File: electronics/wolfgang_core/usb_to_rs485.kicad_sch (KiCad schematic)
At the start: 34 parts

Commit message: Footprints hinzugefügt
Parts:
- U2: renamed from U?; footprint (none) -> Package_QFP:LQFP-64_10x10mm_P0.5mm
- U3, U4, U5, U6: renamed from U?; footprint (none) -> Package_SO:SOIC-8_3.9x4.9mm_P1.27mm
- gave numbers to parts that had none: 23
- renumbered D5 to D1, D6 to D2, D1 to D3, D2 to D4, D3 to D5, D4 to D6
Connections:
- net +5V: now reaches C10.1, U3.8 (VCC)
- net +5V: now also C11.1, C12.1, C13.1, U4.8 (VCC), U5.8 (VCC), U6.8 (VCC)

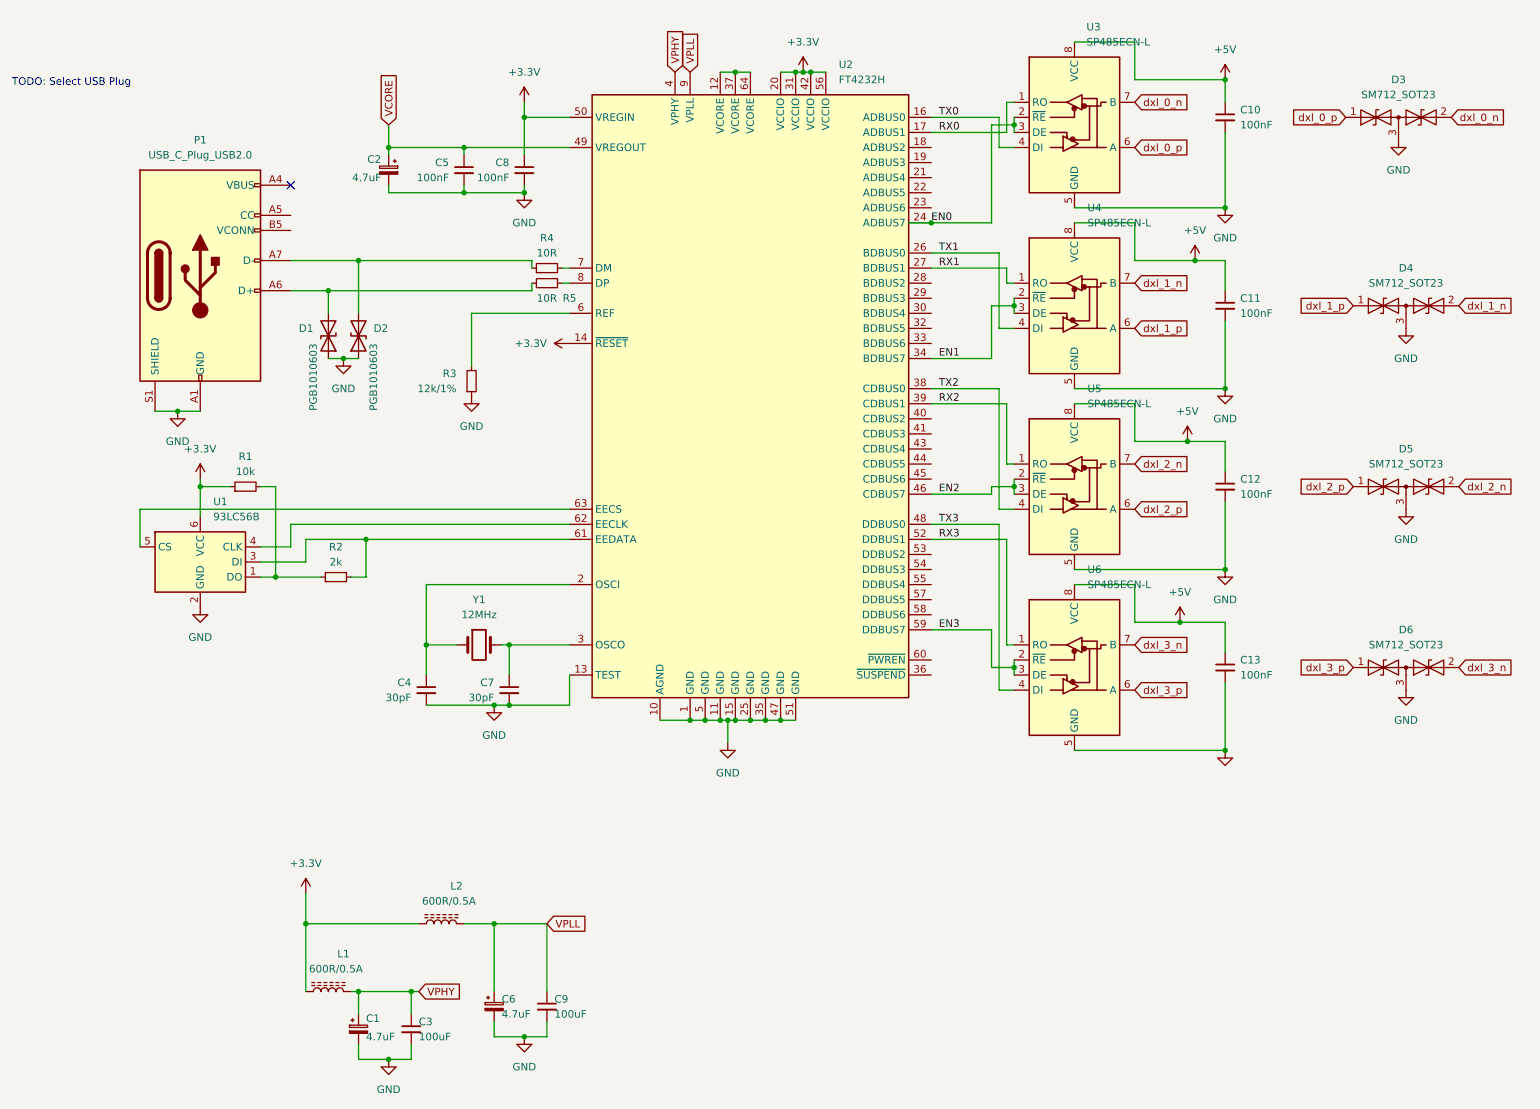
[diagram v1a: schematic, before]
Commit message: Assign almost all Footprints
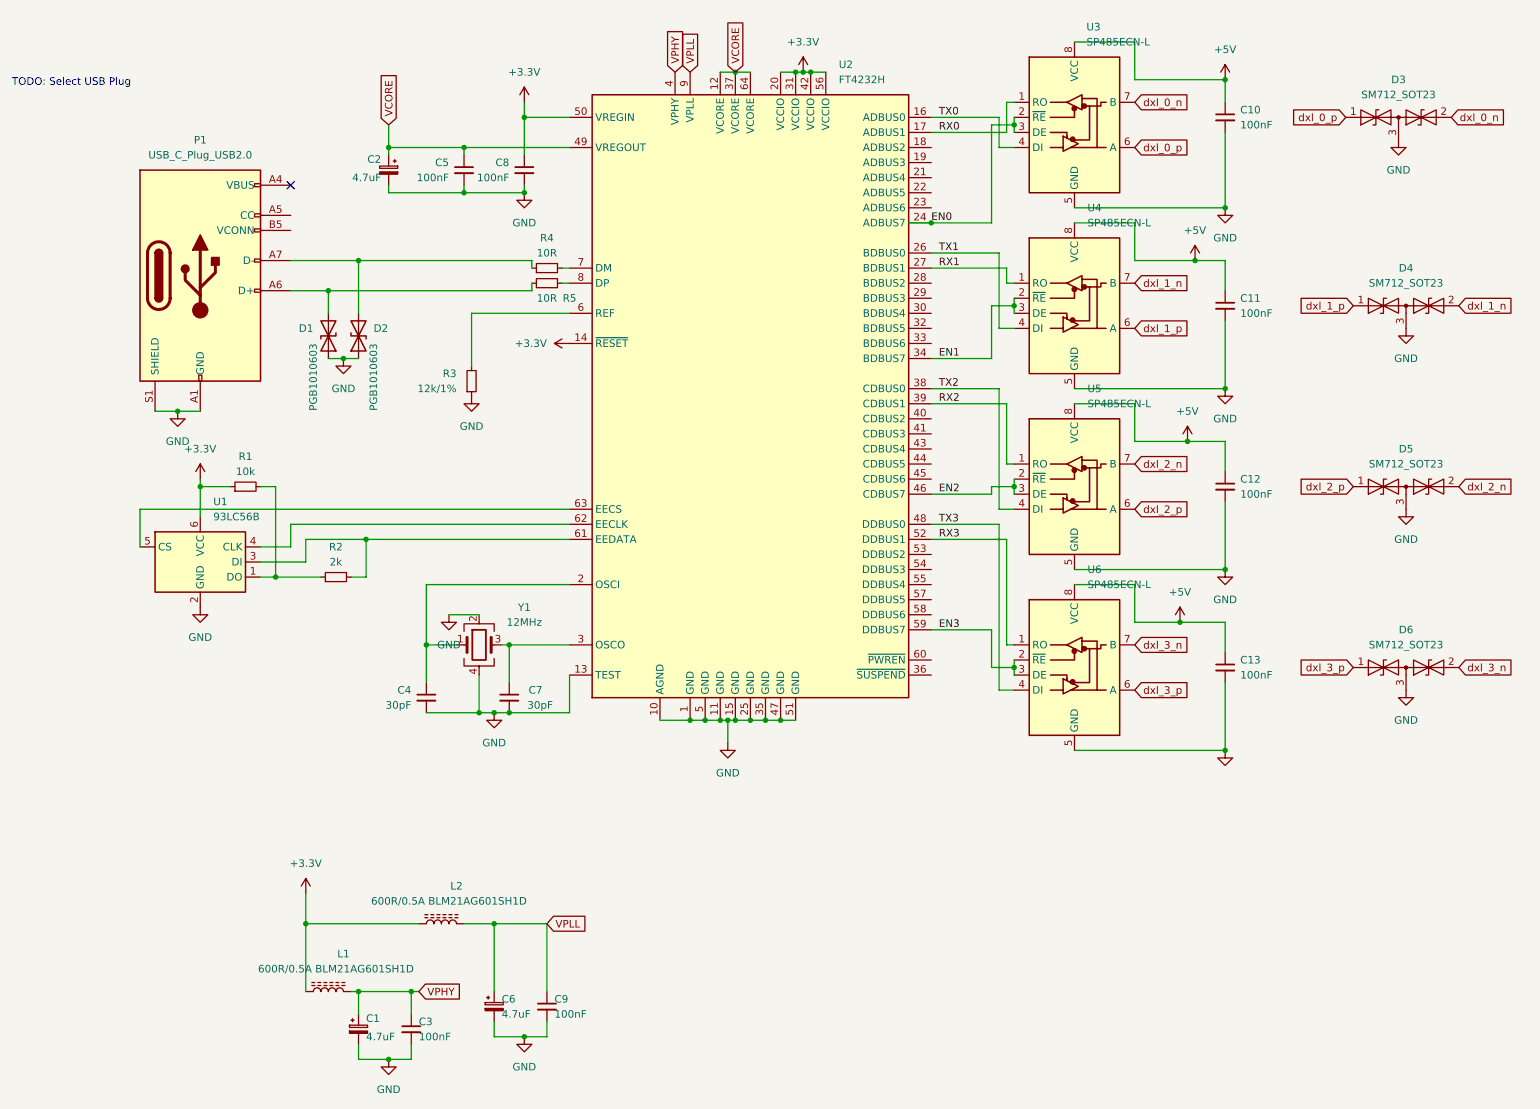
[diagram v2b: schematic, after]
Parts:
- removed Y1: 12MHz, symbol Device:Crystal
- added Y1: 12MHz, Crystal:Crystal_SMD_2520-4Pin_2.5x2.0mm, symbol Device:Crystal_GND24
- C1, C10, C11, C12, C13, C2, C4, C5, C6, C7, C8: footprint (none) -> Capacitor_SMD:C_0805_2012Metric
- C3, C9: value 100uF -> 100nF; footprint (none) -> Capacitor_SMD:C_0805_2012Metric
- D1, D2: footprint (none) -> Diode_SMD:D_0603_1608Metric
- L1, L2: value 600R/0.5A -> 600R/0.5A BLM21AG601SH1D; footprint (none) -> Inductor_SMD:L_0805_2012Metric
- R1, R2, R3, R4, R5: footprint (none) -> Resistor_SMD:R_0805_2012Metric
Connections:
- net GND: now also Y1.2, Y1.4
- net VCORE: now also U2.12 (VCORE), U2.37 (VCORE), U2.64 (VCORE)
- net at C4.1, U2.2 (OSCI): now also Y1.1
- net at C7.1, U2.3 (OSCO): now also Y1.3
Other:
- moved on the sheet: C4, C7
